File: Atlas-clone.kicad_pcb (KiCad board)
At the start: 4 copper layers, 103 x 82.4 mm, 336 parts, among them IC1 PSM712-LF-T7, J1 Conn_01x01, J10 Micro_SD_Card, J11 Conn_01x06, J12 Conn_01x02, J13 USB_B, J14 USB_B, J15 Conn_01x01, J16 Conn_01x01, J2 Conn_01x01, J3 Conn_01x01, J4 Conn_01x32, J5 Conn_01x32, J6 Conn_01x16, J7 Conn_01x16, J8 Conn_02x05_Odd_Even, J9 Conn_01x06, SW1 SW_Push, SW2 SW_Push, U1 TLS115D0E, U10 SN74LVC2G17DB, U1001 VNLD5090, U1002 VNLD5090, U11 SRV05-4, U1101 VNLD5090, U1102 VNLD5090, U12 SRV05-4, U1201 VNLD5090, U1202 VNLD5090, U13 SRV05-4, U14 SN74LVC2G17DB, U15 MCP6004, U16 SRV05-4, U17 MCP6004, U18 SRV05-4, U19 MCP6004, U2 TLS115D0E, U20 SRV05-4, U21 MCP6004, U22 SRV05-4, U23 REF3333, U24 LPS25HB, U26 STM32H753ZIT6, U27 USBLC6-2SC6, U28 S3225SMD32.768KOSC, U3 LMR14020, U4 MCP2551-I-SN, U40 BTS716G, U41 MIC5205-3.3YM5, U42 MIC4427, U43 MIC4427, U44 MIC4427, U45 MIC4427, U46 LM2733XMFX/NOPB, U5 MCP2551-I-SN, U6 AMS1117-3.3, U7 MCP6004, U8 SN74LVC2G17DB, U9 SN74LVC2G17DB, Y1 8MHz

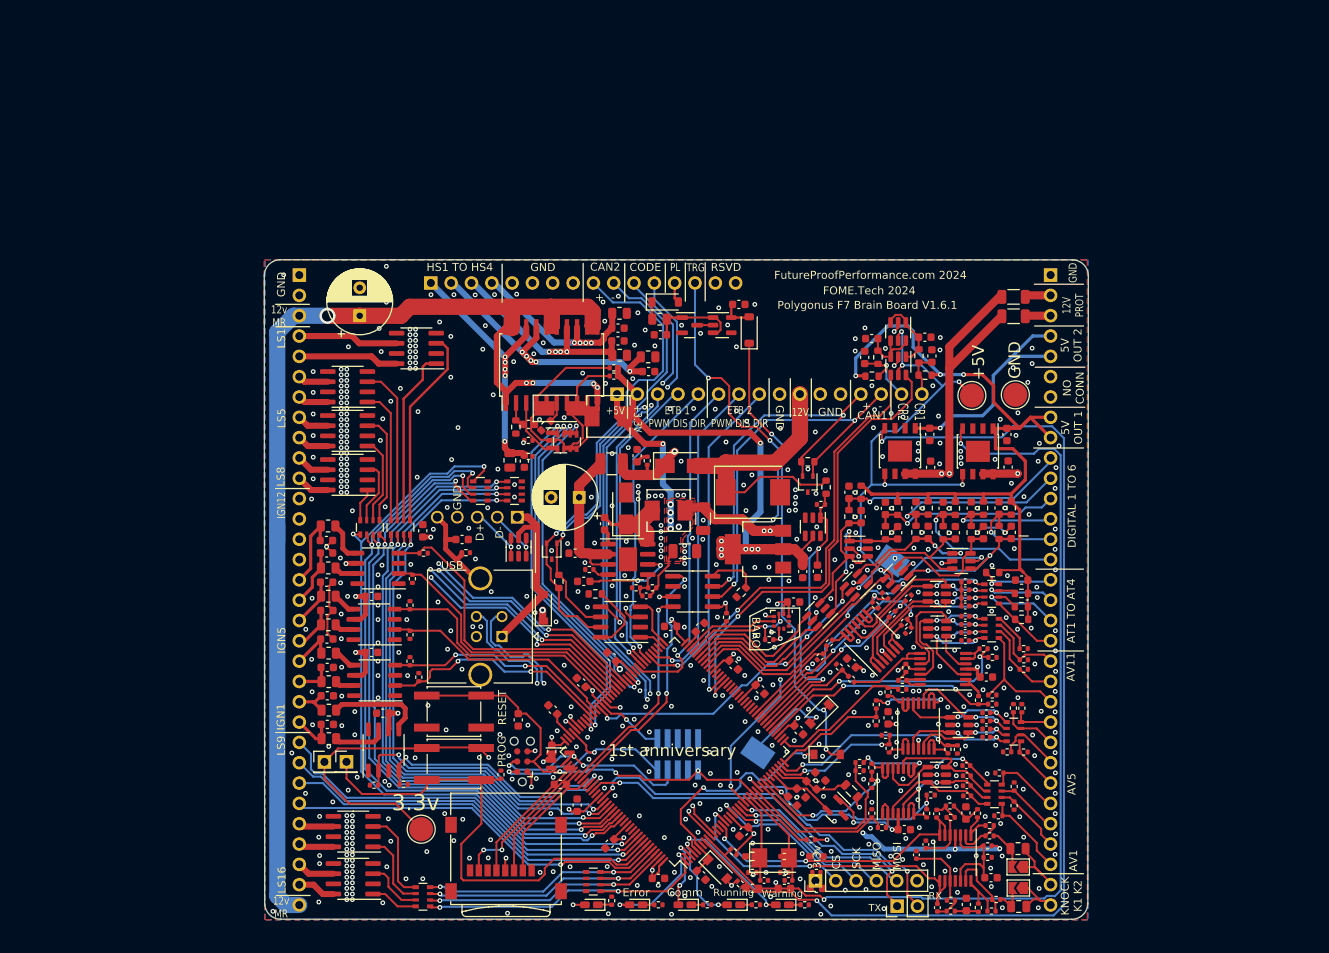
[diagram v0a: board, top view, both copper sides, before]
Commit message: fome-mc: implement integrated motorcycle ECU schematics, 474-part PCB, BOM/CPL, DESIGN.md, and VALIDATION.md
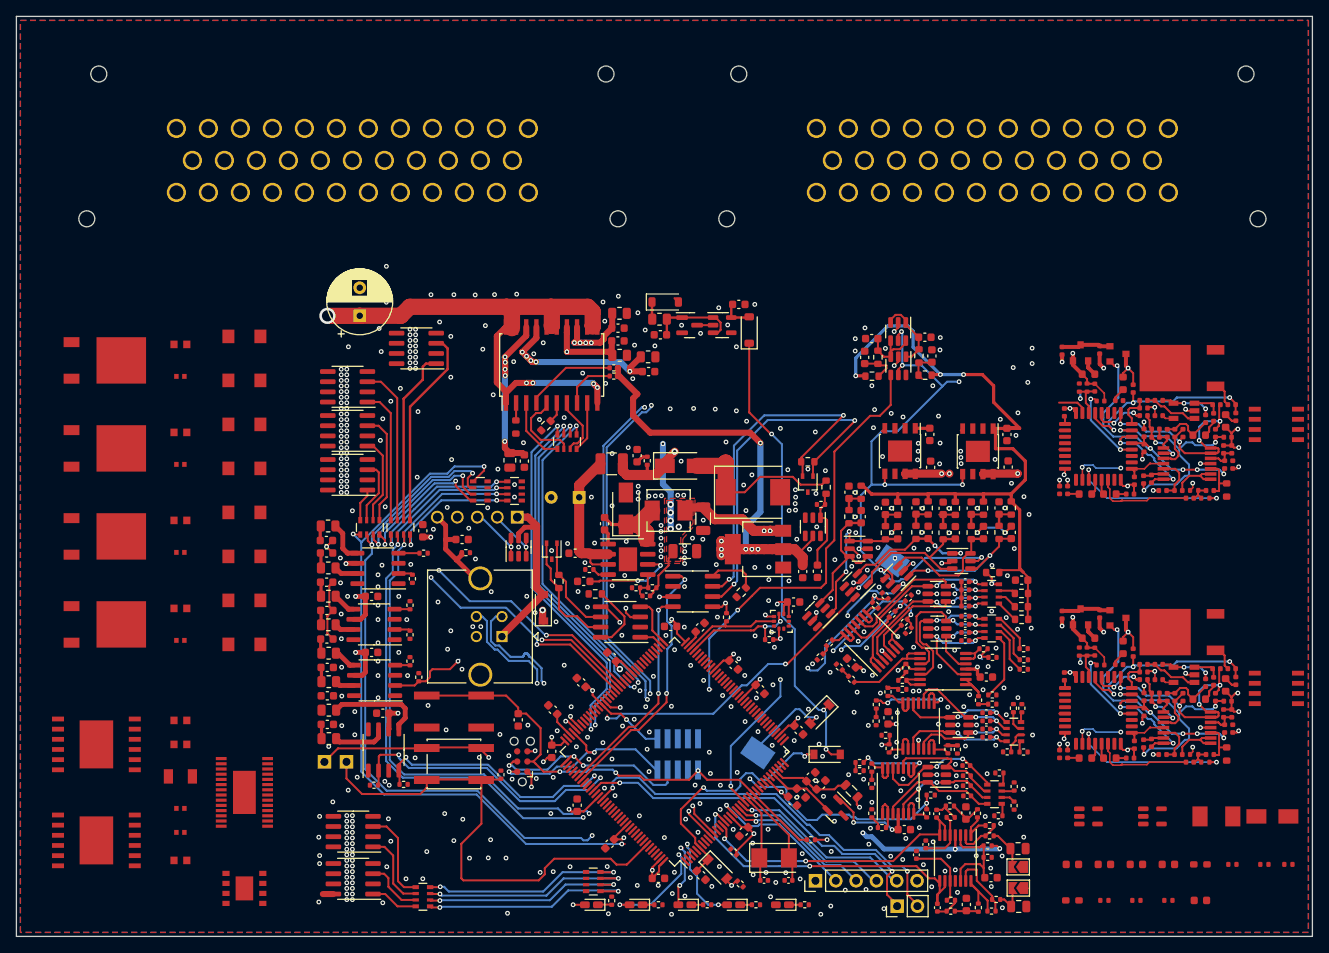
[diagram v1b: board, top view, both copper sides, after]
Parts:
- removed F1, F2: Polyfuse, Resistor_SMD:R_1206_3216Metric
- removed J10: Micro_SD_Card, Connector_Card:microSD_HC_Wuerth_693072010801
- removed J3: Conn_01x01, TestPoint:TestPoint_Pad_D3.0mm
- removed J4, J5: Conn_01x32, Connector_PinHeader_2.54mm:PinHeader_1x32_P2.54mm_Vertical
- removed J6, J7: Conn_01x16, Connector_PinHeader_2.54mm:PinHeader_1x16_P2.54mm_Vertical
- added C1201: 10u, Capacitor_SMD:C_1206_3216Metric, F.Cu at (46.5, 120.0)
- added C201: 10n, Capacitor_SMD:C_0603_1608Metric, F.Cu at (46.5, 113.0)
- added C202: 10n, Capacitor_SMD:C_0603_1608Metric, F.Cu at (46.5, 116.0)
- added C301: 1u, Capacitor_SMD:C_0402_1005Metric, F.Cu at (177.9, 79.1)
- added C302: 100n, Capacitor_SMD:C_0402_1005Metric, F.Cu at (175.2, 84.3)
- added C303: 33n, Capacitor_SMD:C_0402_1005Metric, F.Cu at (168.4, 76.6)
- added C304: 1u, Capacitor_SMD:C_0402_1005Metric, F.Cu at (177.4, 77.6)
- added C305: 100n, Capacitor_SMD:C_0402_1005Metric, F.Cu at (168.8, 74.9)
- added C306: 1u, Capacitor_SMD:C_0402_1005Metric, F.Cu at (160.8, 71.4)
- added C307: 1u, Capacitor_SMD:C_0402_1005Metric, F.Cu at (166.9, 79.0)
- added C308: 100n, Capacitor_SMD:C_0402_1005Metric, F.Cu at (156.7, 66.8)
- added C309: 100n, Capacitor_SMD:C_0402_1005Metric, F.Cu at (166.9, 77.0)
- added C310: 4.7u, Capacitor_SMD:C_0603_1608Metric, F.Cu at (160.0, 69.7)
- added C311: 100n, Capacitor_SMD:C_0402_1005Metric, F.Cu at (166.9, 74.0)
- added C312: 100n, Capacitor_SMD:C_0402_1005Metric, F.Cu at (165.8, 83.0)
- added C313: 100n, Capacitor_SMD:C_0402_1005Metric, F.Cu at (157.0, 74.5)
- added C314: 100n, Capacitor_SMD:C_0402_1005Metric, F.Cu at (178.0, 81.0)
- added C316: 100n, Capacitor_SMD:C_0402_1005Metric, F.Cu at (161.5, 73.1)
- added C317: 1u, Capacitor_SMD:C_0402_1005Metric, F.Cu at (161.4, 66.7)
- added C401: 1u, Capacitor_SMD:C_0402_1005Metric, F.Cu at (177.9, 112.1)
- added C402: 100n, Capacitor_SMD:C_0402_1005Metric, F.Cu at (175.2, 117.3)
- added C403: 33n, Capacitor_SMD:C_0402_1005Metric, F.Cu at (168.4, 109.6)
- added C404: 1u, Capacitor_SMD:C_0402_1005Metric, F.Cu at (177.4, 110.6)
- added C405: 100n, Capacitor_SMD:C_0402_1005Metric, F.Cu at (168.8, 107.9)
- added C406: 1u, Capacitor_SMD:C_0402_1005Metric, F.Cu at (160.8, 104.4)
- added C407: 1u, Capacitor_SMD:C_0402_1005Metric, F.Cu at (166.9, 112.0)
- added C408: 100n, Capacitor_SMD:C_0402_1005Metric, F.Cu at (156.7, 99.8)
- added C409: 100n, Capacitor_SMD:C_0402_1005Metric, F.Cu at (166.9, 110.0)
- added C410: 4.7u, Capacitor_SMD:C_0603_1608Metric, F.Cu at (160.0, 102.7)
- added C411: 100n, Capacitor_SMD:C_0402_1005Metric, F.Cu at (166.9, 107.0)
- added C412: 100n, Capacitor_SMD:C_0402_1005Metric, F.Cu at (165.8, 116.0)
- added C413: 100n, Capacitor_SMD:C_0402_1005Metric, F.Cu at (157.0, 107.5)
- added C414: 100n, Capacitor_SMD:C_0402_1005Metric, F.Cu at (178.0, 114.0)
- added C416: 100n, Capacitor_SMD:C_0402_1005Metric, F.Cu at (161.5, 106.1)
- added C417: 1u, Capacitor_SMD:C_0402_1005Metric, F.Cu at (161.4, 99.7)
- added D201: B340A-13-F, Diode_SMD:D_SMA, F.Cu at (54.5, 65.0)
- added D202: B340A-13-F, Diode_SMD:D_SMA, F.Cu at (54.5, 70.5)
- added D203: B340A-13-F, Diode_SMD:D_SMA, F.Cu at (54.5, 76.0)
- added D204: B340A-13-F, Diode_SMD:D_SMA, F.Cu at (54.5, 81.5)
- added D205: B340A-13-F, Diode_SMD:D_SMA, F.Cu at (54.5, 87.0)
- added D206: B340A-13-F, Diode_SMD:D_SMA, F.Cu at (54.5, 92.5)
- added D207: B340A-13-F, Diode_SMD:D_SMA, F.Cu at (54.5, 98.0)
- added D208: B340A-13-F, Diode_SMD:D_SMA, F.Cu at (54.5, 103.5)
- added D301: RED, LED_SMD:LED_0603_1608Metric, F.Cu at (177.2, 75.6)
- added D302: GREEN, LED_SMD:LED_0603_1608Metric, F.Cu at (162.7, 84.7)
- added D303: BLUE, LED_SMD:LED_0603_1608Metric, F.Cu at (159.6, 84.7)
- added D304: RED, LED_SMD:LED_0603_1608Metric, F.Cu at (164.3, 70.9)
- added D401: RED, LED_SMD:LED_0603_1608Metric, F.Cu at (177.2, 108.6)
- added D402: GREEN, LED_SMD:LED_0603_1608Metric, F.Cu at (162.7, 117.7)
- added D403: BLUE, LED_SMD:LED_0603_1608Metric, F.Cu at (159.6, 117.7)
- added D404: RED, LED_SMD:LED_0603_1608Metric, F.Cu at (164.3, 103.9)
- added Q201: FGD3040G2-F085, Package_TO_SOT_SMD:TO-252-2, F.Cu at (36.0, 68.0)
- added Q202: FGD3040G2-F085, Package_TO_SOT_SMD:TO-252-2, F.Cu at (36.0, 79.0)
- added Q203: FGD3040G2-F085, Package_TO_SOT_SMD:TO-252-2, F.Cu at (36.0, 90.0)
- added Q204: FGD3040G2-F085, Package_TO_SOT_SMD:TO-252-2, F.Cu at (36.0, 101.0)
- added Q301: VND14NV04, Package_TO_SOT_SMD:TO-252-2, F.Cu at (171.7, 69.0)
- added Q401: VND14NV04, Package_TO_SOT_SMD:TO-252-2, F.Cu at (171.7, 102.0)
- added R201: 15R, Resistor_SMD:R_0603_1608Metric, F.Cu at (46.5, 66.0)
- added R202: 15R, Resistor_SMD:R_0603_1608Metric, F.Cu at (46.5, 77.0)
- added R203: 15R, Resistor_SMD:R_0603_1608Metric, F.Cu at (46.5, 88.0)
- added R204: 15R, Resistor_SMD:R_0603_1608Metric, F.Cu at (46.5, 99.0)
- added R205: 10k, Resistor_SMD:R_0402_1005Metric, F.Cu at (46.5, 70.0)
- added R206: 10k, Resistor_SMD:R_0402_1005Metric, F.Cu at (46.5, 81.0)
- added R207: 10k, Resistor_SMD:R_0402_1005Metric, F.Cu at (46.5, 92.0)
- added R208: 10k, Resistor_SMD:R_0402_1005Metric, F.Cu at (46.5, 103.0)
- added R209: 10k, Resistor_SMD:R_0402_1005Metric, F.Cu at (46.5, 127.0)
- added R210: 10k, Resistor_SMD:R_0402_1005Metric, F.Cu at (46.5, 124.0)
- added R212: 2.2k, Resistor_SMD:R_0603_1608Metric, F.Cu at (46.5, 130.5)
- added R301: 1k, Resistor_SMD:R_0402_1005Metric, F.Cu at (177.0, 81.0)
- added R302: 1k, Resistor_SMD:R_0402_1005Metric, F.Cu at (176.9, 79.1)
- added R303: 10k, Resistor_SMD:R_0402_1005Metric, F.Cu at (166.9, 82.9)
- added R304: 10k, Resistor_SMD:R_0402_1005Metric, F.Cu at (171.3, 84.3)
- added R305: 27k, Resistor_SMD:R_0402_1005Metric, F.Cu at (169.3, 84.3)
- added R306: 22k, Resistor_SMD:R_0402_1005Metric, F.Cu at (172.7, 85.2)
- added R307: 27k, Resistor_SMD:R_0402_1005Metric, F.Cu at (167.9, 82.8)
- added R308: 47, Resistor_SMD:R_0402_1005Metric, F.Cu at (169.8, 77.1)
- added R309: 10, Resistor_SMD:R_0402_1005Metric, F.Cu at (175.9, 77.1)
- added R310: 61.9, Resistor_SMD:R_0603_1608Metric, F.Cu at (173.9, 77.3)
- added R311: 10k, Resistor_SMD:R_0402_1005Metric, F.Cu at (174.7, 75.3)
- added R312: 10k, Resistor_SMD:R_0402_1005Metric, F.Cu at (175.7, 75.1)
- added R313: 1k, Resistor_SMD:R_0402_1005Metric, F.Cu at (157.4, 84.2)
- added R314: 62k, Resistor_SMD:R_0603_1608Metric, F.Cu at (177.3, 84.2)
- added R315: 100k, Resistor_SMD:R_0402_1005Metric, F.Cu at (176.0, 73.5)
- added R316: 6.8k, Resistor_SMD:R_0402_1005Metric, F.Cu at (173.2, 84.3)
- added R317: 100k, Resistor_SMD:R_0402_1005Metric, F.Cu at (168.8, 73.0)
- added R318: 1k, Resistor_SMD:R_0402_1005Metric, F.Cu at (163.8, 73.0)
- added R319: 47k, Resistor_SMD:R_0402_1005Metric, F.Cu at (174.6, 85.2)
- added R320: 100k, Resistor_SMD:R_0402_1005Metric, F.Cu at (158.9, 71.4)
- added R321: 10k, Resistor_SMD:R_0402_1005Metric, F.Cu at (159.8, 71.4)
- added R324: 3.3k, Resistor_SMD:R_0402_1005Metric, F.Cu at (166.9, 73.0)
- added R325: 1k, Resistor_SMD:R_0402_1005Metric, F.Cu at (177.9, 73.5)
- added R326: 1k, Resistor_SMD:R_0402_1005Metric, F.Cu at (165.6, 71.5)
- added R327: 1k, Resistor_SMD:R_0402_1005Metric, F.Cu at (178.4, 75.1)
- added R329: 10k, Resistor_SMD:R_0402_1005Metric, F.Cu at (156.4, 84.2)
- added R330: 1k, Resistor_SMD:R_0402_1005Metric, F.Cu at (165.2, 84.7)
- added R331: 68k, Resistor_SMD:R_0402_1005Metric, F.Cu at (166.9, 74.9)
- added R332: 68k, Resistor_SMD:R_0402_1005Metric, F.Cu at (171.8, 77.1)
- added R333: 10k, Resistor_SMD:R_0402_1005Metric, F.Cu at (168.4, 77.6)
- added R334: 10k, Resistor_SMD:R_0402_1005Metric, F.Cu at (170.8, 77.1)
- added R401: 1k, Resistor_SMD:R_0402_1005Metric, F.Cu at (177.0, 114.0)
- added R402: 1k, Resistor_SMD:R_0402_1005Metric, F.Cu at (176.9, 112.1)
- added R403: 10k, Resistor_SMD:R_0402_1005Metric, F.Cu at (166.9, 115.9)
- added R404: 10k, Resistor_SMD:R_0402_1005Metric, F.Cu at (171.3, 117.3)
- added R405: 27k, Resistor_SMD:R_0402_1005Metric, F.Cu at (169.3, 117.3)
- added R406: 22k, Resistor_SMD:R_0402_1005Metric, F.Cu at (172.7, 118.2)
- added R407: 27k, Resistor_SMD:R_0402_1005Metric, F.Cu at (167.9, 115.8)
- added R408: 47, Resistor_SMD:R_0402_1005Metric, F.Cu at (169.8, 110.1)
- added R409: 10, Resistor_SMD:R_0402_1005Metric, F.Cu at (175.9, 110.1)
- added R410: 61.9, Resistor_SMD:R_0603_1608Metric, F.Cu at (173.9, 110.3)
- added R411: 10k, Resistor_SMD:R_0402_1005Metric, F.Cu at (174.7, 108.3)
- added R412: 10k, Resistor_SMD:R_0402_1005Metric, F.Cu at (175.7, 108.1)
- added R413: 1k, Resistor_SMD:R_0402_1005Metric, F.Cu at (157.4, 117.2)
- added R414: 62k, Resistor_SMD:R_0603_1608Metric, F.Cu at (177.3, 117.2)
- added R415: 100k, Resistor_SMD:R_0402_1005Metric, F.Cu at (176.0, 106.5)
- added R416: 6.8k, Resistor_SMD:R_0402_1005Metric, F.Cu at (173.2, 117.3)
- added R417: 100k, Resistor_SMD:R_0402_1005Metric, F.Cu at (168.8, 106.0)
- added R418: 1k, Resistor_SMD:R_0402_1005Metric, F.Cu at (163.8, 106.0)
- added R419: 47k, Resistor_SMD:R_0402_1005Metric, F.Cu at (174.6, 118.2)
- added R420: 100k, Resistor_SMD:R_0402_1005Metric, F.Cu at (158.9, 104.4)
- added R421: 10k, Resistor_SMD:R_0402_1005Metric, F.Cu at (159.8, 104.4)
- added R424: 3.3k, Resistor_SMD:R_0402_1005Metric, F.Cu at (166.9, 106.0)
- added R425: 1k, Resistor_SMD:R_0402_1005Metric, F.Cu at (177.9, 106.5)
- added R426: 1k, Resistor_SMD:R_0402_1005Metric, F.Cu at (165.6, 104.5)
- added R427: 1k, Resistor_SMD:R_0402_1005Metric, F.Cu at (178.4, 108.1)
- added R429: 10k, Resistor_SMD:R_0402_1005Metric, F.Cu at (156.4, 117.2)
- added R430: 1k, Resistor_SMD:R_0402_1005Metric, F.Cu at (165.2, 117.7)
- added R431: 68k, Resistor_SMD:R_0402_1005Metric, F.Cu at (166.9, 107.9)
- added R432: 68k, Resistor_SMD:R_0402_1005Metric, F.Cu at (171.8, 110.1)
- added R433: 10k, Resistor_SMD:R_0402_1005Metric, F.Cu at (168.4, 110.6)
- added R434: 10k, Resistor_SMD:R_0402_1005Metric, F.Cu at (170.8, 110.1)
- added U201: TLE9201SG, Package_SO:Infineon_PG-DSO-12-9, F.Cu at (36.0, 116.0)
- added U202: DRV8825PWPR, Package_SO:HTSSOP-28-1EP_4.4x9.7mm_P0.65mm_EP2.85x5.4mm, F.Cu at (54.5, 122.0)
- added U203: TLE9201SG, Package_SO:Infineon_PG-DSO-12-9, F.Cu at (36.0, 128.0)
- added U25: XTSD04GLGEAG, ampseal:LGA-8_6x8mm_P1.25mm, F.Cu at (54.5, 134.0)
- added U301: MCP6004, Package_SO:TSSOP-14_4.4x5mm_P0.65mm, F.Cu at (172.3, 80.9)
- added U302: STM32F042K6Tx, Package_QFP:LQFP-32_7x7mm_P0.8mm, F.Cu at (161.2, 78.8)
- added U303: REF3033, Package_TO_SOT_SMD:SOT-23, F.Cu at (163.7, 67.2)
- added U305: AD8628, Package_TO_SOT_SMD:TSOT-23-5, F.Cu at (171.9, 74.3)
- added U307: TJA1051T-3, Package_SO:SOIC-8_3.9x4.9mm_P1.27mm, F.Cu at (183.5, 76.0)
- added U309: XC6206P332MR, Package_TO_SOT_SMD:SOT-23, F.Cu at (159.0, 67.1)
- added U401: MCP6004, Package_SO:TSSOP-14_4.4x5mm_P0.65mm, F.Cu at (172.3, 113.9)
- added U402: STM32F042K6Tx, Package_QFP:LQFP-32_7x7mm_P0.8mm, F.Cu at (161.2, 111.8)
- added U403: REF3033, Package_TO_SOT_SMD:SOT-23, F.Cu at (163.7, 100.2)
- added U405: AD8628, Package_TO_SOT_SMD:TSOT-23-5, F.Cu at (171.9, 107.3)
- added U407: TJA1051T-3, Package_SO:SOIC-8_3.9x4.9mm_P1.27mm, F.Cu at (183.5, 109.0)
- added U409: XC6206P332MR, Package_TO_SOT_SMD:SOT-23, F.Cu at (159.0, 100.1)
- D10, D11, D12, D13, D9: footprint LED_SMD:LED_0603_1608Metric_Castellated -> LED_SMD:LED_0603_1608Metric
- J1: value Conn_01x01 -> TE_776163-1; footprint TestPoint:TestPoint_Pad_D3.0mm -> ampseal:ampseal-35
- J2: value Conn_01x01 -> TE_776163-2; footprint TestPoint:TestPoint_Pad_D3.0mm -> ampseal:ampseal-35-2
- moved C107 102.9 mm to (174.0, 135.5)
- moved D18 102.6 mm to (183.0, 125.0)
- moved R123 97.4 mm to (170.0, 135.5)
- moved R122 95.3 mm to (166.0, 135.5)
- moved L3 91.0 mm to (176.0, 125.0)
- moved J1 87.9 mm to (68.0, 43.0)
- moved U46 87.7 mm to (168.0, 125.0)
- moved C106 76.7 mm to (170.0, 131.0)
- moved U28 66.4 mm to (160.0, 125.0)
- moved R119 63.0 mm to (185.0, 131.0)
- moved R117 60.0 mm to (178.0, 131.0)
- moved R118 60.0 mm to (182.0, 131.0)
- moved R116 56.0 mm to (174.0, 131.0)
- moved C103 40.1 mm to (158.0, 131.0)
- moved C104 40.1 mm to (162.0, 131.0)
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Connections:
- net /lowside_quad4/IN1 renamed /PB8_STEP_EN
- net /mcu/BOOT0 renamed /BOOT0_NET
- C106 pad 1: +3V3 -> Net-(U28-GND)
- C106 pad 2: GND -> unconnected-(C106-Pad2)
- C107 pad 1: /12V_PROT -> unconnected-(C107-Pad1)
- C107 pad 2: GND -> Net-(U46-IN)
- C6 pad 1: Net-(U3-EN) -> /VBOOST
- C7 pad 1: Net-(U3-EN) -> /VBOOST
- D18 pad 1: Net-(U3-EN) -> unconnected-(D18-K-Pad1)
- D18 pad 2: Net-(U46-SW) -> Net-(D18-A)
- J1 pad 1: GND -> /LS1
- J2 pad 1: +5V -> /AT1
- L1 pad 2: Net-(U3-EN) -> /VBOOST
- L3 pad 1: /12V_PROT -> unconnected-(L3-Pad1)
- L3 pad 2: Net-(U46-SW) -> Net-(D18-A)
- R122 pad 1: Net-(U3-EN) -> Net-(U46-OUT)
- R122 pad 2: Net-(U46-FB) -> unconnected-(R122-Pad2)
- R123 pad 1: Net-(U46-FB) -> unconnected-(R123-Pad1)
- R123 pad 2: GND -> unconnected-(R123-Pad2)
- U26 pad 1: unconnected-(U26-PE2-Pad1) -> /WBO1_NRST
- U26 pad 2: unconnected-(U26-PE3-Pad2) -> /WBO1_BOOT0
- U26 pad 3: unconnected-(U26-PE4-Pad3) -> /WBO2_NRST
- U26 pad 4: unconnected-(U26-PE5-Pad4) -> /WBO2_BOOT0
- U28 pad 1: +3V3 -> unconnected-(U28-IN-Pad1)
- U28 pad 2: GND -> Net-(U28-GND)
- U28 pad 3: /mcu/LSE_32K -> unconnected-(U28-EN-Pad3)
- U28 pad 4: +3V3 -> unconnected-(U28-BP-Pad4)
- U28 pad 5: +3V3 -> unconnected-(U28-OUT-Pad5)
- U3 pad 2: Net-(U3-EN) -> /VBOOST
- U3 pad 3: Net-(U3-EN) -> /VBOOST
- U46 pad 1: Net-(U46-SW) -> Net-(U46-IN)
- U46 pad 2: GND -> unconnected-(U46-GND-Pad2)
- U46 pad 3: Net-(U46-FB) -> unconnected-(U46-EN-Pad3)
- U46 pad 4: /12V_PROT -> unconnected-(U46-BP-Pad4)
- U46 pad 5: /12V_PROT -> Net-(U46-OUT)
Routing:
- net /mcu/5V_SENSOR_2_PG: track 134.2 -> 0.51 mm, vias 2 -> 0
- net /mcu/5V_SENSOR_1_PG: track 119.0 -> 0.33 mm, vias 2 -> 0
- net /12V_MR: track 152.1 -> 69.2 mm
- net /RC1: track 81.2 -> 0.00 mm, vias 4 -> 0
- net /RC2: track 80.4 -> 0.00 mm, vias 4 -> 0
- net GND: track 40.6 -> 120.6 mm, vias 568 -> 560
- net /lowside_quad2/IN2: track 82.8 -> 19.4 mm, vias 3 -> 2
- net VDDA: track 0.00 -> 62.8 mm, vias 0 -> 10
- net /lowside_quad2/IN1: track 80.1 -> 18.3 mm, vias 3 -> 2
- net /mcu/LED1: track 14.5 -> 74.9 mm, vias 2 -> 5
- net /lowside_quad1/IN4: track 80.2 -> 19.9 mm, vias 3 -> 2
- net /mcu/VR_1: track 58.6 -> 0.18 mm, vias 2 -> 0
- net /IGN12: track 50.1 -> 0.00 mm, vias 2 -> 0
- net /LS9: track 49.8 -> 0.00 mm, vias 1 -> 0
- net /mcu/UART_RX: track 49.4 -> 0.00 mm, vias 2 -> 0
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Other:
- board size 103 x 82.4 mm -> 162 x 115 mm
- board text added: "BARO POTTING DAM KEEP-OUT (ID 8mm / OD 11mm -> ePTFE VENT)"
- board text removed: "+ -"
- board text removed: "+3.3V"
- board text removed: "+5V"
- board text removed: "12V"
- board text removed: "12V PROT"
- board text removed: "12v MR"
- board text removed: "1st anniversary"
- board text removed: "3.3v"
- board text removed: "5V OUT 1"
- board text removed: "5V OUT 2"
- board text removed: "AT1 TO AT4"
- board text removed: "AV1"
- board text removed: "AV11"
- board text removed: "AV5"
- board text removed: "BARO"
- board text removed: "CAN1"
- board text removed: "CAN2"
- board text removed: "CODE"
- board text removed: "CR1 CR2"
- board text removed: "CS"
- board text removed: "Comm"
- board text removed: "D+"
- board text removed: "D-"
- board text removed: "DIGITAL 1 TO 6"
- board text removed: "ETB 1 PWM DIS DIR"
- board text removed: "ETB 2 PWM DIS DIR"
- board text removed: "Error"
- board text removed: "FOME.Tech 2024"
- board text removed: "FutureProofPerformance.com 2024"
- board text removed: "GND"
- board text removed: "HS1 TO HS4"
- board text removed: "IGN1"
- board text removed: "IGN12"
- board text removed: "IGN5"
- board text removed: "KNOCK K1 K2"
- board text removed: "LS1"
- board text removed: "LS16"
- board text removed: "LS5"
- board text removed: "LS8"
- board text removed: "LS9"
- board text removed: "MISO"
- board text removed: "MOSI"
- board text removed: "NO CONN"
- board text removed: "PL"
- board text removed: "PROG"
- board text removed: "Polygonus F7 Brain Board V1.6.1"
- board text removed: "RESET"
- board text removed: "RSVD"
- board text removed: "RX"
- board text removed: "Running"
- board text removed: "SCK"
- board text removed: "TRG"
- board text removed: "TX"
- board text removed: "USB"
- board text removed: "USB B"
- board text removed: "Warning"
